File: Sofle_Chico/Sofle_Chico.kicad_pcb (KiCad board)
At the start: 2 copper layers, 145.4 x 116.3 mm, 116 parts, among them J1 Conn_01x05, J2 4PIN, J3 Conn_01x04, J4 Conn_01x04, J5 Conn_01x05, J6 Conn_01x05, J7 Conn_01x04, SW1 SW_PUSH, SW10 SW_PUSH, SW11 SW_PUSH, SW12 SW_PUSH, SW13 SW_PUSH, SW14 SW_PUSH, SW15 SW_PUSH, SW16 SW_PUSH, SW17 SW_PUSH, SW18 SW_PUSH, SW19 SW_PUSH_LED, SW2 SW_PUSH, SW20 SW_PUSH, SW21 SW_PUSH, SW22 SW_PUSH, SW23 SW_PUSH, SW24 SW_PUSH, SW25 SW_PUSH, SW26 SW_PUSH, SW27 SW_PUSH, SW28 SW_PUSH, SW29 SW_PUSH, SW3 SW_PUSH, SW30 SW_PUSH, SW4 SW_PUSH, SW5 SW_PUSH, SW6 SW_PUSH, SW7 SW_PUSH, SW8 SW_PUSH, SW9 SW_PUSH, U1 SN74AHCT1G125, U2 Pico

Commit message: Painfully figuring out how to Fork and unfork myself
Fixed busted footprints and lost SCH changes from Git goof-ups. Discovering what I've failed to properly put into version control & tinkering
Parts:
- SW20: renamed from SW19; value SW_PUSH_LED -> SW_PUSH
- SW25: footprint Sofle_Pico:SW_Hotswap_Kailh_Choc_V1V2_DS_1.00u_1 -> Sofle_Pico:RotaryEncoder_Alps_EC11E-Switch_Vertical_H20mm-keebio_modified
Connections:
- net Net-(D31-A) renamed VBUS
- D31 pad 1: +5V -> VCC
- LED1 pad 1: VCC -> GND
- LED1 pad 2: Net-(LED1-DOUT) -> Net-(JP1-B)
- LED1 pad 3: GND -> VCC
- LED1 pad 4: Net-(JP1-B) -> Net-(LED1-DOUT)
- LED10 pad 1: VCC -> GND
- LED10 pad 2: Net-(LED10-DOUT) -> Net-(LED10-DIN)
- LED10 pad 3: GND -> VCC
- LED10 pad 4: Net-(LED10-DIN) -> Net-(LED10-DOUT)
- LED11 pad 1: VCC -> GND
- LED11 pad 2: Net-(LED11-DOUT) -> Net-(LED10-DOUT)
- LED11 pad 3: GND -> VCC
- LED11 pad 4: Net-(LED10-DOUT) -> Net-(LED11-DOUT)
- LED12 pad 1: VCC -> GND
- LED12 pad 2: Net-(LED12-DOUT) -> Net-(LED11-DOUT)
- LED12 pad 3: GND -> VCC
- LED12 pad 4: Net-(LED11-DOUT) -> Net-(LED12-DOUT)
- LED13 pad 1: VCC -> GND
- LED13 pad 2: Net-(LED13-DOUT) -> Net-(LED12-DOUT)
- LED13 pad 3: GND -> VCC
- LED13 pad 4: Net-(LED12-DOUT) -> Net-(LED13-DOUT)
- LED14 pad 1: VCC -> GND
- LED14 pad 2: Net-(LED14-DOUT) -> Net-(LED13-DOUT)
- LED14 pad 3: GND -> VCC
- LED14 pad 4: Net-(LED13-DOUT) -> Net-(LED14-DOUT)
- LED15 pad 1: VCC -> GND
- LED15 pad 2: Net-(LED15-DOUT) -> Net-(LED14-DOUT)
- LED15 pad 3: GND -> VCC
- LED15 pad 4: Net-(LED14-DOUT) -> Net-(LED15-DOUT)
- LED16 pad 1: VCC -> GND
- LED16 pad 2: Net-(LED16-DOUT) -> Net-(LED15-DOUT)
- LED16 pad 3: GND -> VCC
- LED16 pad 4: Net-(LED15-DOUT) -> Net-(LED16-DOUT)
- LED17 pad 1: VCC -> GND
- LED17 pad 2: Net-(LED17-DOUT) -> Net-(LED16-DOUT)
- LED17 pad 3: GND -> VCC
- LED17 pad 4: Net-(LED16-DOUT) -> Net-(LED17-DOUT)
- LED18 pad 1: VCC -> GND
- LED18 pad 2: Net-(LED18-DOUT) -> Net-(LED17-DOUT)
- LED18 pad 3: GND -> VCC
- LED18 pad 4: Net-(LED17-DOUT) -> Net-(LED18-DOUT)
- LED19 pad 1: VCC -> GND
- LED19 pad 2: Net-(LED19-DOUT) -> Net-(LED18-DOUT)
- LED19 pad 3: GND -> VCC
- LED19 pad 4: Net-(LED18-DOUT) -> Net-(LED19-DOUT)
- LED2 pad 1: VCC -> GND
- LED2 pad 2: Net-(LED2-DOUT) -> Net-(LED1-DOUT)
- LED2 pad 3: GND -> VCC
- LED2 pad 4: Net-(LED1-DOUT) -> Net-(LED2-DOUT)
- LED20 pad 1: VCC -> GND
- LED20 pad 2: Net-(LED20-DOUT) -> Net-(LED19-DOUT)
- LED20 pad 3: GND -> VCC
- LED20 pad 4: Net-(LED19-DOUT) -> Net-(LED20-DOUT)
- LED21 pad 1: VCC -> GND
- LED21 pad 2: Net-(LED21-DOUT) -> Net-(LED20-DOUT)
- LED21 pad 3: GND -> VCC
- LED21 pad 4: Net-(LED20-DOUT) -> Net-(LED21-DOUT)
- LED22 pad 1: VCC -> GND
- LED22 pad 2: Net-(LED22-DOUT) -> Net-(LED21-DOUT)
- LED22 pad 3: GND -> VCC
- LED22 pad 4: Net-(LED21-DOUT) -> Net-(LED22-DOUT)
- LED23 pad 1: VCC -> GND
- LED23 pad 2: Net-(LED23-DOUT) -> Net-(LED22-DOUT)
- LED23 pad 3: GND -> VCC
- LED23 pad 4: Net-(LED22-DOUT) -> Net-(LED23-DOUT)
- LED24 pad 1: VCC -> GND
- LED24 pad 2: Net-(LED24-DOUT) -> Net-(LED23-DOUT)
- LED24 pad 3: GND -> VCC
- LED24 pad 4: Net-(LED23-DOUT) -> Net-(LED24-DOUT)
- LED25 pad 1: VCC -> GND
- LED25 pad 2: Net-(LED25-DOUT) -> Net-(LED24-DOUT)
- LED25 pad 3: GND -> VCC
- LED25 pad 4: Net-(LED24-DOUT) -> Net-(LED25-DOUT)
- LED26 pad 1: VCC -> GND
- LED26 pad 2: Net-(LED26-DOUT) -> Net-(LED25-DOUT)
- LED26 pad 3: GND -> VCC
- LED26 pad 4: Net-(LED25-DOUT) -> Net-(LED26-DOUT)
- LED27 pad 1: VCC -> GND
- LED27 pad 2: Net-(LED27-DOUT) -> Net-(LED26-DOUT)
- LED27 pad 3: GND -> VCC
- LED27 pad 4: Net-(LED26-DOUT) -> Net-(LED27-DOUT)
- LED28 pad 1: VCC -> GND
- LED28 pad 2: Net-(LED28-DOUT) -> Net-(LED27-DOUT)
- LED28 pad 3: GND -> VCC
- LED28 pad 4: Net-(LED27-DOUT) -> Net-(LED28-DOUT)
- LED29 pad 1: VCC -> GND
- LED29 pad 2: unconnected-(LED29-DOUT-Pad2) -> Net-(LED28-DOUT)
- LED29 pad 3: GND -> VCC
- LED29 pad 4: Net-(LED28-DOUT) -> unconnected-(LED29-DOUT-Pad4)
- LED3 pad 1: VCC -> GND
- LED3 pad 2: Net-(LED3-DOUT) -> Net-(LED2-DOUT)
- LED3 pad 3: GND -> VCC
- LED3 pad 4: Net-(LED2-DOUT) -> Net-(LED3-DOUT)
- LED4 pad 1: VCC -> GND
- LED4 pad 2: Net-(LED4-DOUT) -> Net-(LED3-DOUT)
- LED4 pad 3: GND -> VCC
- LED4 pad 4: Net-(LED3-DOUT) -> Net-(LED4-DOUT)
- LED5 pad 1: VCC -> GND
- LED5 pad 2: Net-(LED5-DOUT) -> Net-(LED4-DOUT)
- LED5 pad 3: GND -> VCC
- LED5 pad 4: Net-(LED4-DOUT) -> Net-(LED5-DOUT)
- LED6 pad 1: VCC -> GND
- LED6 pad 2: Net-(LED6-DOUT) -> Net-(LED5-DOUT)
- LED6 pad 3: GND -> VCC
- LED6 pad 4: Net-(LED5-DOUT) -> Net-(LED6-DOUT)
- LED7 pad 1: VCC -> GND
- LED7 pad 2: Net-(LED7-DOUT) -> Net-(LED6-DOUT)
- LED7 pad 3: GND -> VCC
- LED7 pad 4: Net-(LED6-DOUT) -> Net-(LED7-DOUT)
- LED8 pad 1: VCC -> GND
- LED8 pad 2: Net-(LED8-DOUT) -> Net-(LED7-DOUT)
- LED8 pad 3: GND -> VCC
- LED8 pad 4: Net-(LED7-DOUT) -> Net-(LED8-DOUT)
- LED9 pad 1: VCC -> GND
- LED9 pad 2: Net-(LED10-DIN) -> Net-(LED8-DOUT)
- LED9 pad 3: GND -> VCC
- LED9 pad 4: Net-(LED8-DOUT) -> Net-(LED10-DIN)
- U2 pad 39: +5V -> VCC
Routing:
- net Net-(LED17-DOUT): track 0.00 -> 28.5 mm, vias 0 -> 1
- net Net-(LED16-DOUT): track 28.5 -> 0.00 mm, vias 1 -> 0
- net Net-(LED6-DOUT): track 13.5 -> 0.00 mm
- net (no net): track 0.00 -> 13.5 mm
- net VCC: track 63.8 -> 73.9 mm
- net +5V: track 10.1 -> 0.00 mm
- added copper zone on B.Cu, net VCC
- removed copper zone on B.Cu, net +5V

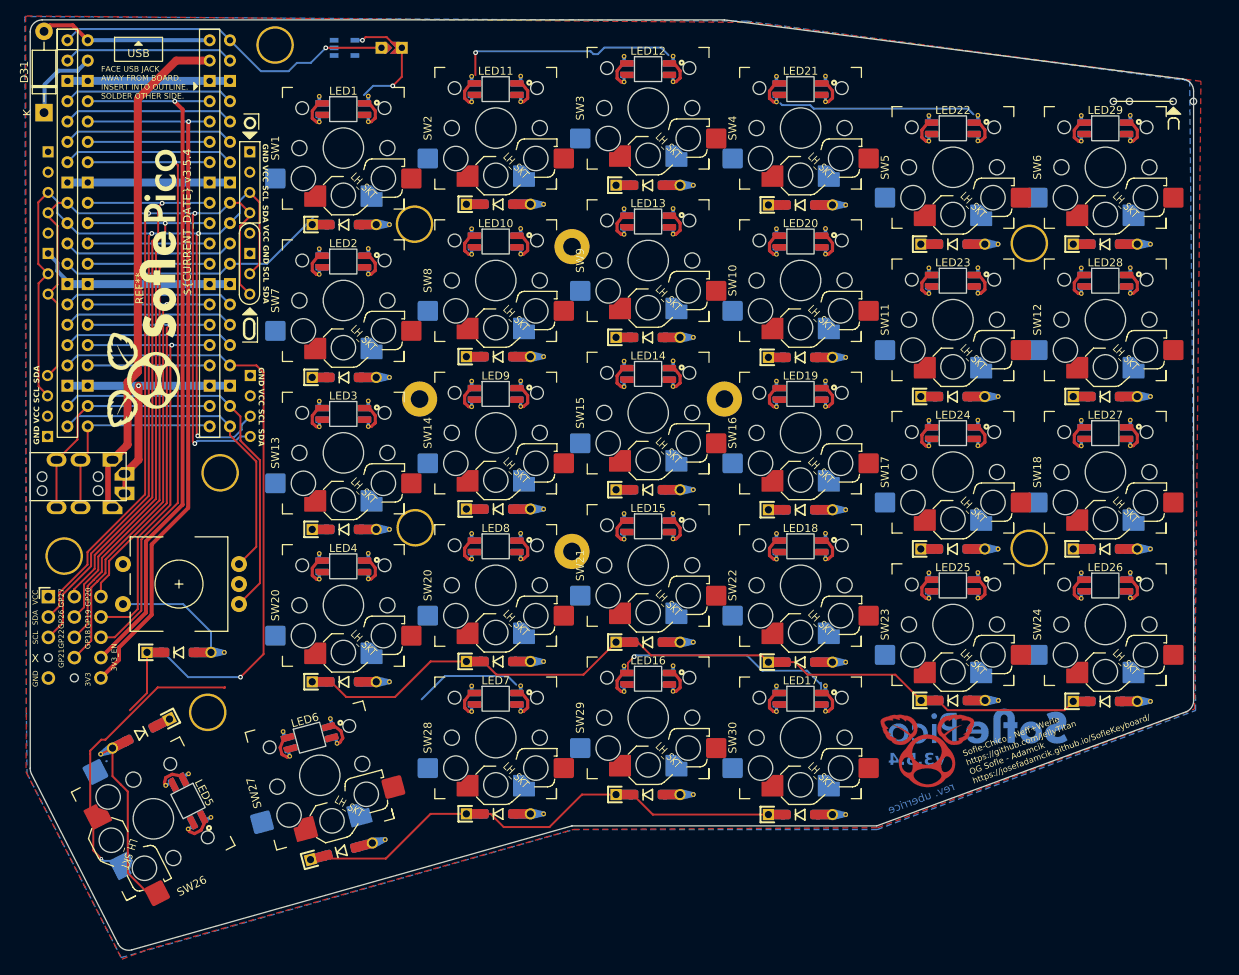
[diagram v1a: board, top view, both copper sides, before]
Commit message: Routing progress.
Cleaned up STEP model links for relative paths

Implemented first pass at PFET power-split protection

tinkering with LED footprints

Fixed unintentionally altered annotation
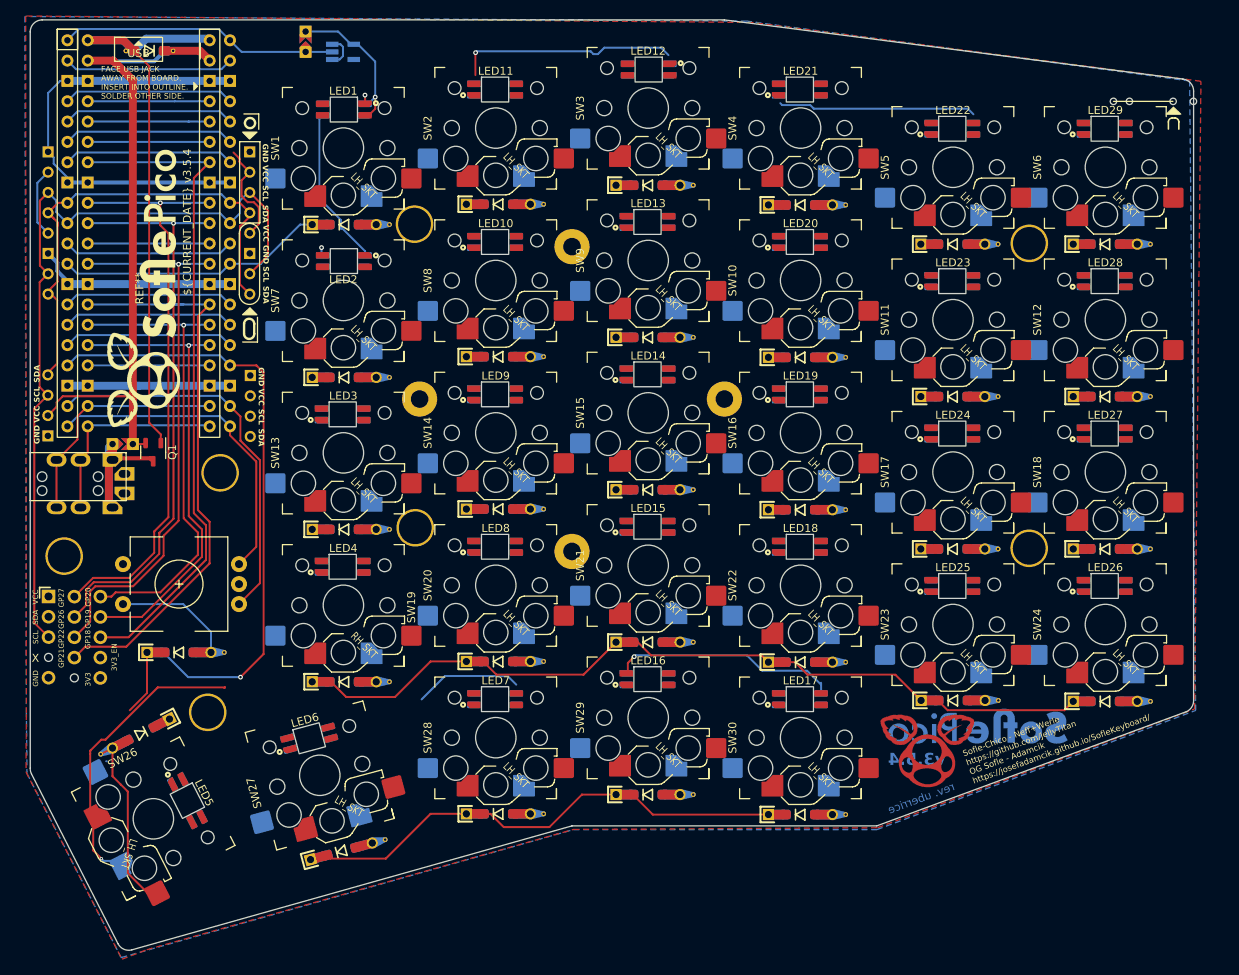
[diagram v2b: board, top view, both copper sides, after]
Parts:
- removed the SW20 at (120.5, 107.2)
- removed TH7: HOLE, Sofle_Pico:Hole from sofle for M2 posts gold rimmer wide-keyplate-hole
- added JP2: SolderJumper_2_Open, Sofle_Pico:Level Shifter Bypass Jumper, F.Cu at (93.0, 87.0)
- added Q1: DMG2305UX, Package_TO_SOT_SMD:SOT-23-3, F.Cu at (96.8, 88.0)
- added SW19: SW_PUSH, Sofle_Pico:SW_Hotswap_Kailh_Choc_V1V2_DS_1.00u_1, F.Cu at (120.5, 107.2)
- D31: value 1N5817 -> MBR120VLSF; footprint Diode_THT:D_DO-41_SOD81_P10.16mm_Horizontal -> Sofle_Pico:D_SOD-123_DO-41_Hybrid_DoubleSided_V2_1
- JP1: value Level shifter bypass jumper -> SolderJumper_2_Open
- LED1, LED12: moved to F.Cu
- SW25: value SW_PUSH -> Rotary_Encoder_Switch-Device
- U1: footprint Sofle_Pico:SN74AHCT1G125 -> PCM_Package_TO_SOT_SMD_AKL:SOT-23-5_HandSoldering
- moved D31 15.2 mm to (96.3, 37.8), turned to 180 degrees
- moved JP1 10.8 mm to (115.8, 36.7), turned to 90 degrees
- moved U1 0.53 mm to (120.5, 38.0)
- moved J7 0.09 mm to (83.6, 82.2)
- moved J6 0.07 mm to (90.2, 106.1)
- turned LED1 to 0 degrees
- turned LED12 to 0 degrees
- turned LED2 to 0 degrees
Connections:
- J2 pad 2: VCC -> Net-(JP2-A)
- SW20 pad 1: SW25A -> col4
- SW20 pad 2: Net-(D19-A) -> Net-(D20-A)
- SW21 pad 1: col4 -> col3
- SW21 pad 2: Net-(D20-A) -> Net-(D21-A)
- SW22 pad 1: col3 -> col2
- SW22 pad 2: Net-(D21-A) -> Net-(D22-A)
- SW23 pad 1: col2 -> col1
- SW23 pad 2: Net-(D22-A) -> Net-(D23-A)
- SW24 pad 1: col1 -> col0
- SW24 pad 2: Net-(D23-A) -> Net-(D24-A)
- SW25 pad A: (no net) -> ENCA
- SW25 pad B: (no net) -> ENCB
- SW25 pad C: (no net) -> GND
- SW25 pad S1: (no net) -> SW25A
- SW25 pad S2: (no net) -> SW25B
- SW26 pad 1: col4 -> Net-(D26-A)
- SW26 pad 2: Net-(D26-A) -> col4
- U1 pad 5: VCC -> unconnected-(U1-VCC-Pad5)
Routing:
- net SDA: track 151.8 -> 61.1 mm, vias 3 -> 0
- net 3V3_EN: track 89.4 -> 15.2 mm, vias 1 -> 0
- net 3V3: track 89.3 -> 15.2 mm, vias 1 -> 0
- net SCL: track 158.6 -> 101.3 mm, vias 3 -> 0
- net VBUS: track 21.8 -> 73.5 mm
- net col4: track 59.2 -> 21.3 mm, vias 1 -> 0
- net Net-(D26-A): track 22.9 -> 60.7 mm, vias 0 -> 1
- net VCC: track 73.9 -> 111.2 mm, vias 0 -> 1
- net Net-(JP2-A): track 0.00 -> 23.0 mm
- net Net-(LED1-DOUT): track 0.00 -> 20.3 mm
- net LED: track 44.3 -> 34.8 mm, vias 1 -> 0
- net GP21: track 64.2 -> 72.7 mm, vias 1 -> 0
- net GND: track 99.9 -> 106.2 mm
- net GP20: track 52.8 -> 59.0 mm
- net Net-(JP1-B): track 15.3 -> 19.4 mm, vias 2 -> 1
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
